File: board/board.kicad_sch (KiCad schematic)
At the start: 3 parts, among them J1 004_BASE-T_CT, J2 013_PoE_rectified

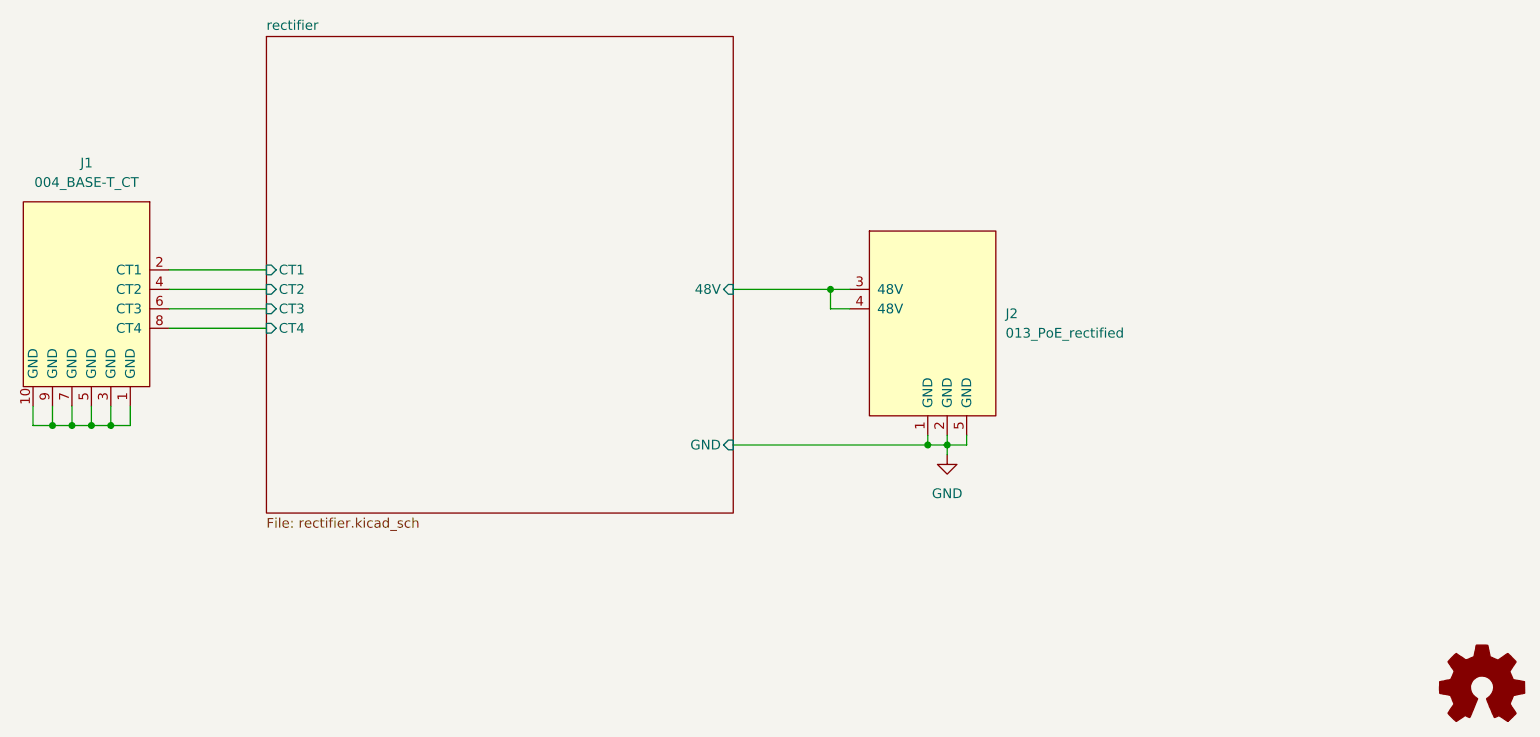
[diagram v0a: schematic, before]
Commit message: updated to v1.0 of put_on_edge
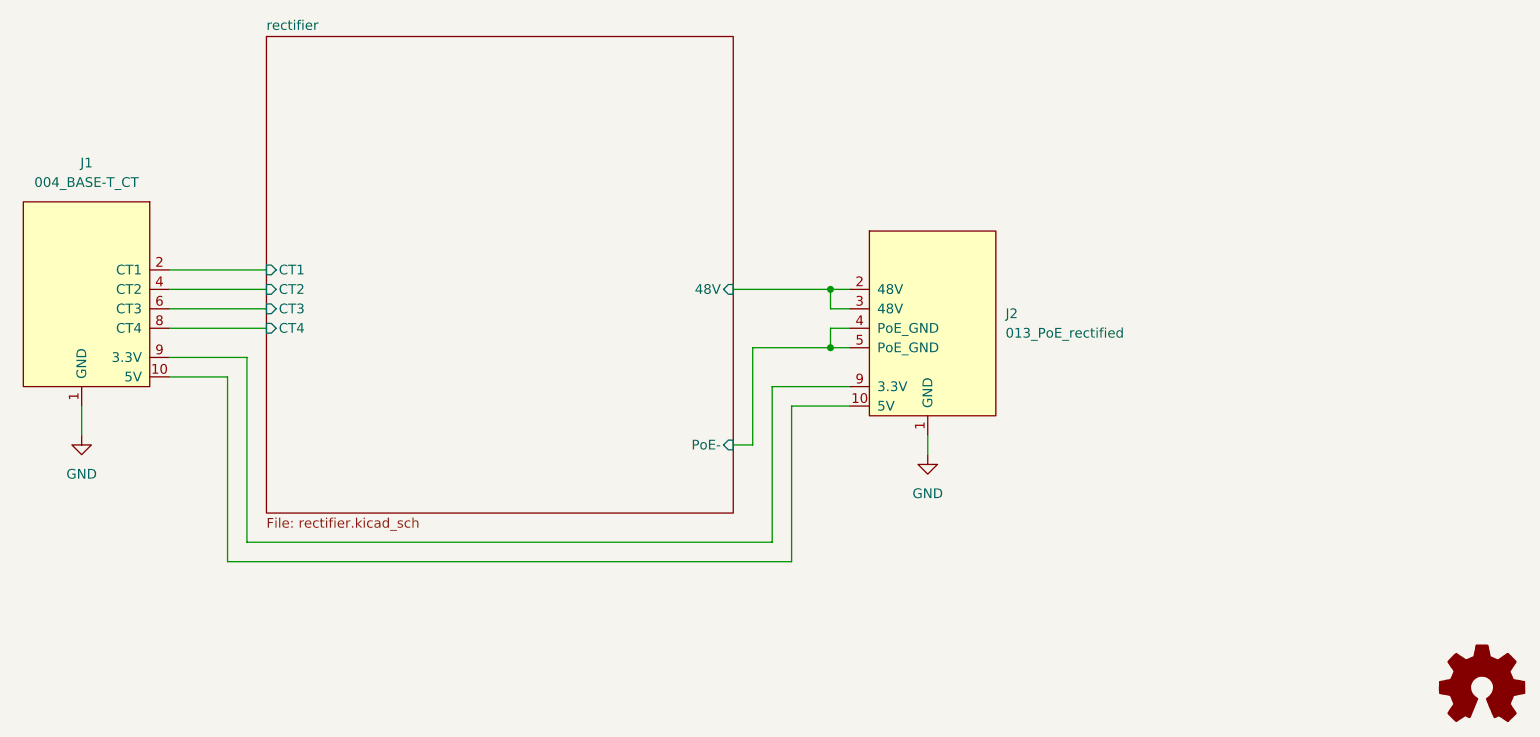
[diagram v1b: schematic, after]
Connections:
- net GND: now also J1.1 (GND); no longer J2.2 (GND), J2.5 (GND)
- net rectifier/48V: now also J2.2 (48V); no longer J2.4 (48V)
- new net: J1.10 (5V), J2.10 (5V)
- new net: J1.9 (3.3V), J2.9 (3.3V)
- new net rectifier/PoE-: J2.4 (PoE_GND), J2.5 (PoE_GND)
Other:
- sheet rectifier ports: added PoE-; removed GND
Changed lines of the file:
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@@
   (junction (at 187.96 105.41) (diameter 0) (color 0 0 0 0)
   )
-  (junction (at 203.2 125.73) (diameter 0) (color 0 0 0 0)
-  )
-  (junction (at 88.9 123.19) (diameter 0) (color 0 0 0 0)
-  )
-  (junction (at 91.44 123.19) (diameter 0) (color 0 0 0 0)
-  )
-  (junction (at 93.98 123.19) (diameter 0) (color 0 0 0 0)
-  )
-  (junction (at 200.66 125.73) (diameter 0) (color 0 0 0 0)
-  )
-  (junction (at 86.36 123.19) (diameter 0) (color 0 0 0 0)
-  )
-  (wire (pts (xy 93.98 123.19) (xy 96.52 123.19))
-    (stroke (width 0) (type default) (color 0 0 0 0))
+  (junction (at 187.96 113.03) (diameter 0) (color 0 0 0 0)
   )
   (wire (pts (xy 101.6 105.41) (xy 114.3 105.41))
     (stroke (width 0) (type default) (color 0 0 0 0))
   )
-  (wire (pts (xy 88.9 120.65) (xy 88.9 123.19))
+  (wire (pts (xy 90.17 120.65) (xy 90.17 124.46))
+    (stroke (width 0) (type default) (color 0 0 0 0))
+  )
+  (wire (pts (xy 109.22 116.84) (xy 101.6 116.84))
     (stroke (width 0) (type default) (color 0 0 0 0))
   )
@@
     (stroke (width 0) (type default) (color 0 0 0 0))
   )
-  (wire (pts (xy 203.2 125.73) (xy 203.2 127))
-    (stroke (width 0) (type default) (color 0 0 0 0))
-  )
-  (wire (pts (xy 175.26 125.73) (xy 200.66 125.73))
-    (stroke (width 0) (type default) (color 0 0 0 0))
-  )
-  (wire (pts (xy 200.66 125.73) (xy 203.2 125.73))
-    (stroke (width 0) (type default) (color 0 0 0 0))
-  )
-  (wire (pts (xy 205.74 124.46) (xy 205.74 125.73))
-    (stroke (width 0) (type default) (color 0 0 0 0))
-  )
-  (wire (pts (xy 91.44 123.19) (xy 93.98 123.19))
-    (stroke (width 0) (type default) (color 0 0 0 0))
-  )
-  (wire (pts (xy 93.98 120.65) (xy 93.98 123.19))
+  (wire (pts (xy 190.5 110.49) (xy 187.96 110.49))
+    (stroke (width 0) (type default) (color 0 0 0 0))
+  )
+  (wire (pts (xy 182.88 120.65) (xy 182.88 140.97))
+    (stroke (width 0) (type default) (color 0 0 0 0))
+  )
+  (wire (pts (xy 182.88 140.97) (xy 109.22 140.97))
+    (stroke (width 0) (type default) (color 0 0 0 0))
+  )
+  (wire (pts (xy 101.6 114.3) (xy 111.76 114.3))
+    (stroke (width 0) (type default) (color 0 0 0 0))
+  )
+  (wire (pts (xy 109.22 140.97) (xy 109.22 116.84))
+    (stroke (width 0) (type default) (color 0 0 0 0))
+  )
+  (wire (pts (xy 180.34 138.43) (xy 180.34 118.11))
+    (stroke (width 0) (type default) (color 0 0 0 0))
+  )
+  (wire (pts (xy 177.8 113.03) (xy 187.96 113.03))
+    (stroke (width 0) (type default) (color 0 0 0 0))
+  )
+  (wire (pts (xy 111.76 114.3) (xy 111.76 138.43))
+    (stroke (width 0) (type default) (color 0 0 0 0))
+  )
+  (wire (pts (xy 177.8 125.73) (xy 177.8 113.03))
     (stroke (width 0) (type default) (color 0 0 0 0))
   )
@@
     (stroke (width 0) (type default) (color 0 0 0 0))
   )
-  (wire (pts (xy 205.74 125.73) (xy 203.2 125.73))
-    (stroke (width 0) (type default) (color 0 0 0 0))
-  )
-  (wire (pts (xy 200.66 124.46) (xy 200.66 125.73))
-    (stroke (width 0) (type default) (color 0 0 0 0))
-  )
-  (wire (pts (xy 86.36 120.65) (xy 86.36 123.19))
+  (wire (pts (xy 175.26 125.73) (xy 177.8 125.73))
+    (stroke (width 0) (type default) (color 0 0 0 0))
+  )
+  (wire (pts (xy 111.76 138.43) (xy 180.34 138.43))
+    (stroke (width 0) (type default) (color 0 0 0 0))
+  )
+  (wire (pts (xy 187.96 113.03) (xy 190.5 113.03))
     (stroke (width 0) (type default) (color 0 0 0 0))
   )
@@
     (stroke (width 0) (type default) (color 0 0 0 0))
   )
-  (wire (pts (xy 86.36 123.19) (xy 88.9 123.19))
+  (wire (pts (xy 180.34 118.11) (xy 190.5 118.11))
+    (stroke (width 0) (type default) (color 0 0 0 0))
+  )
+  (wire (pts (xy 200.66 124.46) (xy 200.66 127))
     (stroke (width 0) (type default) (color 0 0 0 0))
   )
@@
     (stroke (width 0) (type default) (color 0 0 0 0))
   )
-  (wire (pts (xy 96.52 123.19) (xy 96.52 120.65))
+  (wire (pts (xy 187.96 110.49) (xy 187.96 113.03))
     (stroke (width 0) (type default) (color 0 0 0 0))
   )
@@
     (stroke (width 0) (type default) (color 0 0 0 0))
   )
-  (wire (pts (xy 91.44 120.65) (xy 91.44 123.19))
-    (stroke (width 0) (type default) (color 0 0 0 0))
-  )
-  (wire (pts (xy 88.9 123.19) (xy 91.44 123.19))
-    (stroke (width 0) (type default) (color 0 0 0 0))
-  )
-  (wire (pts (xy 83.82 120.65) (xy 83.82 123.19))
-    (stroke (width 0) (type default) (color 0 0 0 0))
-  )
-  (wire (pts (xy 83.82 123.19) (xy 86.36 123.19))
-    (stroke (width 0) (type default) (color 0 0 0 0))
-  )
-  (wire (pts (xy 203.2 125.73) (xy 203.2 124.46))
+  (wire (pts (xy 190.5 120.65) (xy 182.88 120.65))
     (stroke (width 0) (type default) (color 0 0 0 0))
   )
@@
     )
     (property "Datasheet" "" (id 3) (at 82.55 90.17 0)
+      (effects (font (size 1.27 1.27)) hide)
+    )
+    (pin "1")
+    (pin "10")
+    (pin "2")
+    (pin "4")
+    (pin "6")
+    (pin "8")
+    (pin "9")
+  )
+  (symbol (lib_id "power:GND") (at 90.17 124.46 0) (unit 1)
+    (in_bom yes) (on_board yes) (fields_autoplaced)
+    (property "Reference" "#PWR0101" (id 0) (at 90.17 130.81 0)
+      (effects (font (size 1.27 1.27)) hide)
+    )
+    (property "Value" "GND" (id 1) (at 90.17 129.54 0))
+    (property "Footprint" "" (id 2) (at 90.17 124.46 0)
+      (effects (font (size 1.27 1.27)) hide)
+    )
+    (property "Datasheet" "" (id 3) (at 90.17 124.46 0)
+      (effects (font (size 1.27 1.27)) hide)
+    )
+    (pin "1")
+  )
+  (symbol (lib_id "power:GND") (at 200.66 127 0) (unit 1)
+    (in_bom yes) (on_board yes) (fields_autoplaced)
+    (property "Reference" "#PWR0102" (id 0) (at 200.66 133.35 0)
+      (effects (font (size 1.27 1.27)) hide)
+    )
+    (property "Value" "GND" (id 1) (at 200.66 132.08 0))
+    (property "Footprint" "" (id 2) (at 200.66 127 0)
+      (effects (font (size 1.27 1.27)) hide)
+    )
+    (property "Datasheet" "" (id 3) (at 200.66 127 0)
+      (effects (font (size 1.27 1.27)) hide)
+    )
+    (pin "1")
+  )
+  (symbol (lib_id "Graphic:Logo_Open_Hardware_Small") (at 273.05 157.48 0) (unit 1)
+    (in_bom yes) (on_board yes) (fields_autoplaced)
+    (property "Reference" "LOGO1" (id 0) (at 273.05 150.495 0)
+      (effects (font (size 1.27 1.27)) hide)
+    )
+    (property "Value" "Logo_Open_Hardware_Small" (id 1) (at 273.05 163.195 0)
+      (effects (font (size 1.27 1.27)) hide)
+    )
+    (property "Footprint" "Symbol:OSHW-Symbol_6.7x6mm_SilkScreen" (id 2) (at 273.05 157.48 0)
+      (effects (font (size 1.27 1.27)) hide)
+    )
+    (property "Datasheet" "~" (id 3) (at 273.05 157.48 0)
+      (effects (font (size 1.27 1.27)) hide)
+    )
+  )
+  (symbol (lib_id "put_on_edge:013_PoE_rectified") (at 201.93 110.49 0) (unit 1)
+    (in_bom yes) (on_board yes) (fields_autoplaced)
+    (property "Reference" "J2" (id 0) (at 210.82 108.5849 0)
+      (effects (font (size 1.27 1.27)) (justify left))
+    )
+    (property "Value" "013_PoE_rectified" (id 1) (at 210.82 111.1249 0)
+      (effects (font (size 1.27 1.27)) (justify left))
+    )
+    (property "Footprint" "on_edge:on_edge_2x05_host" (id 2) (at 209.55 93.98 0)
+      (effects (font (size 1.27 1.27)) hide)
+    )
+    (property "Datasheet" "" (id 3) (at 209.55 93.98 0)
       (effects (font (size 1.27 1.27)) hide)
     )
@@
     (pin "4")
     (pin "5")
-    (pin "6")
-    (pin "7")
-    (pin "8")
     (pin "9")
-  )
-  (symbol (lib_id "power:GND") (at 203.2 127 0) (unit 1)
-    (in_bom yes) (on_board yes) (fields_autoplaced)
-    (property "Reference" "#PWR0101" (id 0) (at 203.2 133.35 0)
-      (effects (font (size 1.27 1.27)) hide)
-    )
-    (property "Value" "GND" (id 1) (at 203.2 132.08 0))
-    (property "Footprint" "" (id 2) (at 203.2 127 0)
-      (effects (font (size 1.27 1.27)) hide)
-    )
-    (property "Datasheet" "" (id 3) (at 203.2 127 0)
-      (effects (font (size 1.27 1.27)) hide)
-    )
-    (pin "1")
-  )
-  (symbol (lib_id "Graphic:Logo_Open_Hardware_Small") (at 273.05 157.48 0) (unit 1)
-    (in_bom yes) (on_board yes) (fields_autoplaced)
-    (property "Reference" "LOGO1" (id 0) (at 273.05 150.495 0)
-      (effects (font (size 1.27 1.27)) hide)
-    )
-    (property "Value" "Logo_Open_Hardware_Small" (id 1) (at 273.05 163.195 0)
-      (effects (font (size 1.27 1.27)) hide)
-    )
-    (property "Footprint" "Symbol:OSHW-Symbol_6.7x6mm_SilkScreen" (id 2) (at 273.05 157.48 0)
-      (effects (font (size 1.27 1.27)) hide)
-    )
-    (property "Datasheet" "~" (id 3) (at 273.05 157.48 0)
-      (effects (font (size 1.27 1.27)) hide)
-    )
-  )
-  (symbol (lib_id "put_on_edge:013_PoE_rectified") (at 201.93 110.49 0) (unit 1)
-    (in_bom yes) (on_board yes) (fields_autoplaced)
-    (property "Reference" "J2" (id 0) (at 210.82 108.5849 0)
-      (effects (font (size 1.27 1.27)) (justify left))
-    )
-    (property "Value" "013_PoE_rectified" (id 1) (at 210.82 111.1249 0)
-      (effects (font (size 1.27 1.27)) (justify left))
-    )
-    (property "Footprint" "on_edge:on_edge_2x05_host" (id 2) (at 209.55 93.98 0)
-      (effects (font (size 1.27 1.27)) hide)
-    )
-    (property "Datasheet" "" (id 3) (at 209.55 93.98 0)
-      (effects (font (size 1.27 1.27)) hide)
-    )
-    (pin "1")
-    (pin "2")
-    (pin "3")
-    (pin "4")
-    (pin "5")
   )
   (sheet (at 114.3 72.39) (size 60.96 62.23) (fields_autoplaced)
@@
       (effects (font (size 1.27 1.27)) (justify left top))
     )
-    (pin "GND" input (at 175.26 125.73 0)
+    (pin "PoE-" input (at 175.26 125.73 0)
       (effects (font (size 1.27 1.27)) (justify right))
     )
@@
       (reference "#PWR0101") (unit 1) (value "GND") (footprint "")
     )
+    (path "/8d1c5e87-55c6-47eb-b9c7-30ff69c4aa16"
+      (reference "#PWR0102") (unit 1) (value "GND") (footprint "")
+    )
     (path "/767ce4c6-0e55-4543-92f0-34cb8237a544/7f5f8093-49f9-4dd2-8910-45ffcd8f5757"
